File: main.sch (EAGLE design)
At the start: 26 parts, among them IC1 FT232RL, U1 ATMEGA328P_TQFP, Y3 16MHz

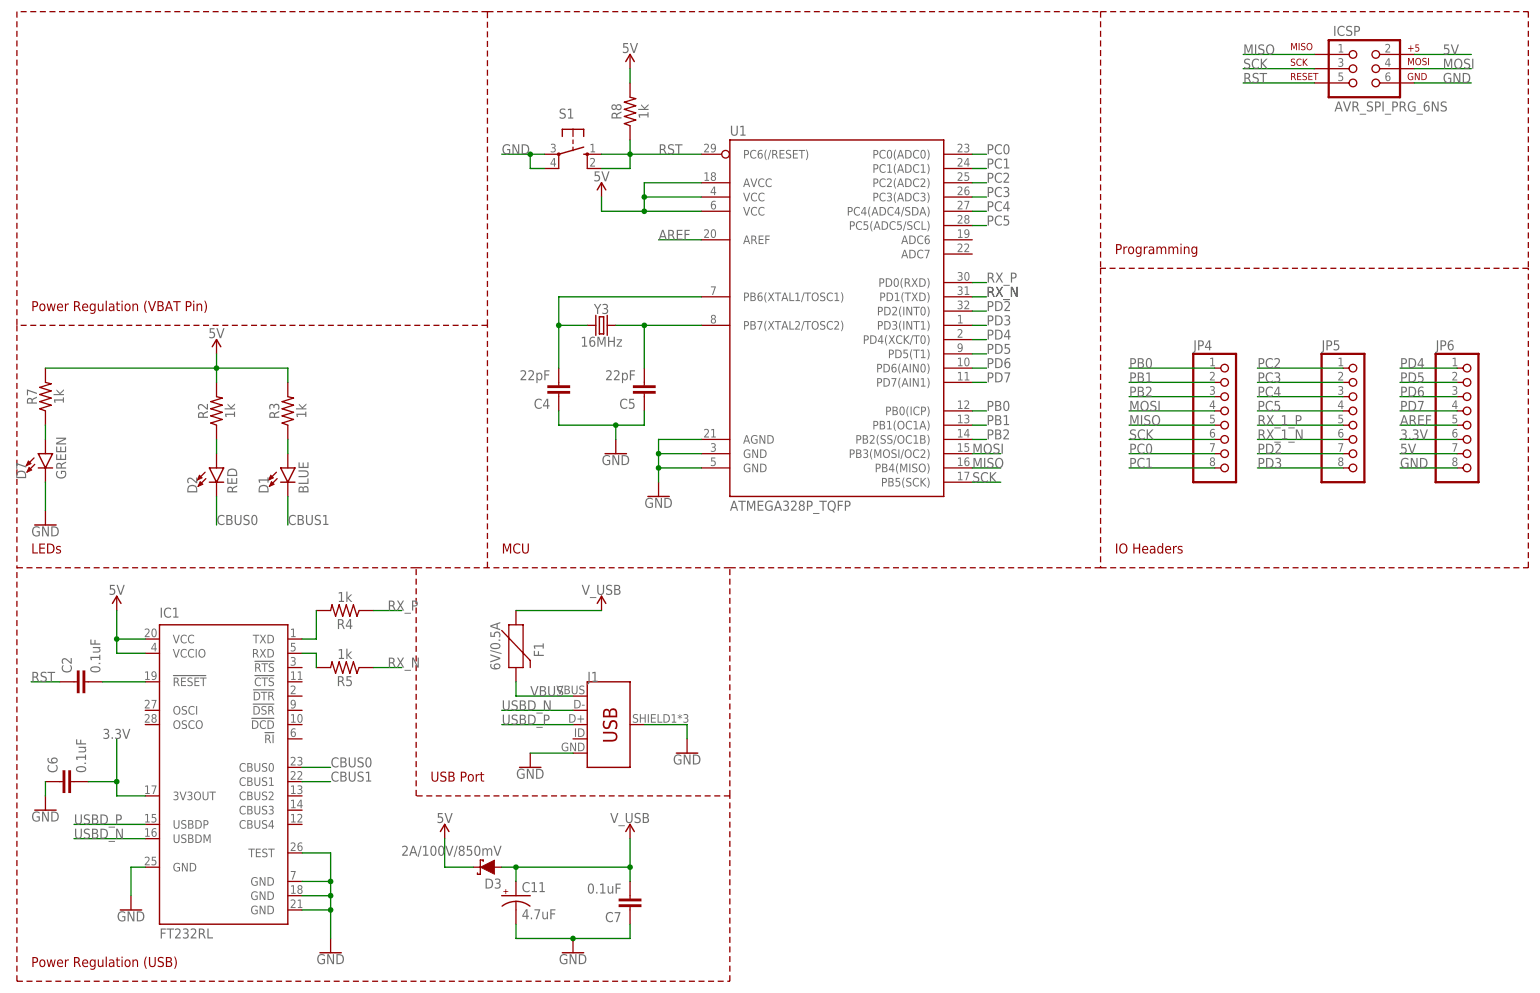
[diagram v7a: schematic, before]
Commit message: 8/1/17 - Used new ATMEGA32U4
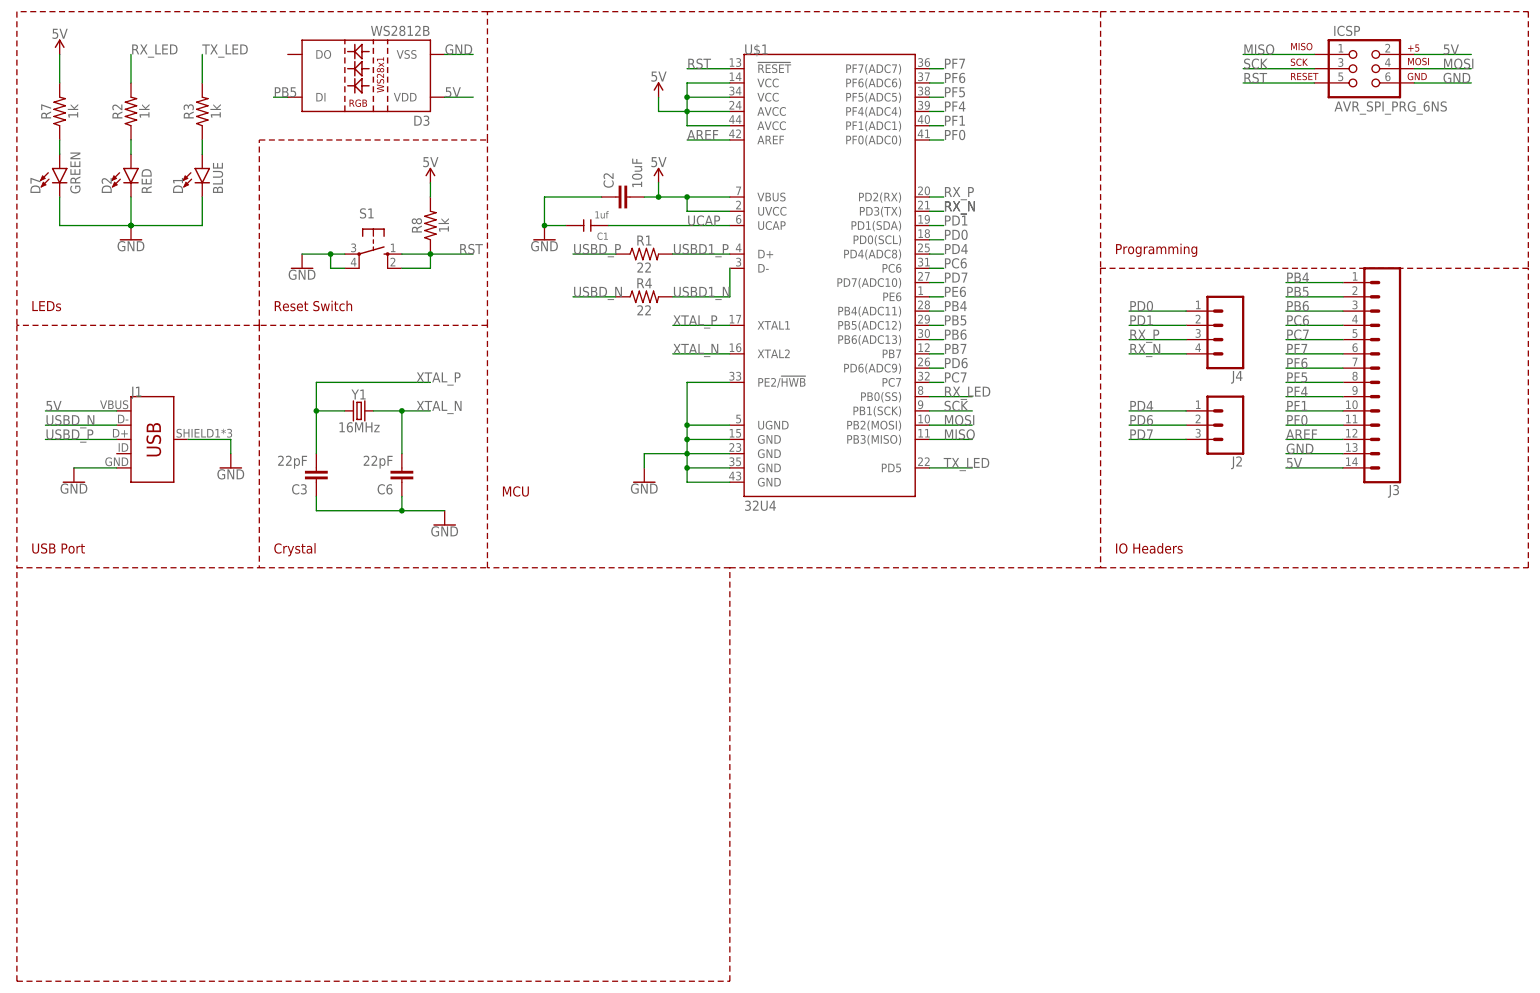
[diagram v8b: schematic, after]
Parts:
- removed C11: 4.7uF, SparkFun-Capacitors:10UF-POLAR-0603-6.3V-20%(TANT)
- removed C4, C5: 22pF, SparkFun-Capacitors:22PF-0603-50V-5%
- removed C7: 0.1uF, SparkFun-Capacitors:0.1UF-0603-25V-5%
- removed F1: 6V/0.5A, SparkFun-Fuses:PPTC_HALF-AMP
- removed IC1: FT232RL, ftdichip:FT232RL
- removed JP4, JP5, JP6: (no value), pinhead:PINHD-1X8
- removed R5: 1k, SparkFun-Resistors:RESISTOR0805
- removed U1: ATMEGA328P_TQFP, SparkFun-IC-Microcontroller:ATMEGA328P_TQFP
- removed Y3: 16MHz, SparkFun-Clocks:CRYSTAL-16MHZPTH-HC49US
- added C1: 1uf, Seeed-Capacitor:CERAMIC-1UF-25V-10%-X7R(0603)
- added C3: 22pF, SparkFun-Capacitors:22PF-0603-50V-5%
- added J2: (no value), SparkFun-Connectors:CONN_03
- added J3: (no value), SparkFun-Connectors:CONN_14
- added J4: (no value), SparkFun-Connectors:CONN_04
- added R1: 22, SparkFun-Resistors:22OHM-0603-1/10W-1%
- added U$1: 32U4, SparkFun-IC-Microcontroller:ATMEGA32U4TQFP-44
- added Y1: 16MHz, SparkFun-Clocks:CRYSTAL-16MHZPTH-HC49US
- C2: value 0.1uF -> 10uF; device SparkFun-Capacitors:0.1UF-0603-25V-5% -> SparkFun-Capacitors:10UF-0805-10V-10%
- C6: value 0.1uF -> 22pF; device SparkFun-Capacitors:0.1UF-0603-25V-5% -> SparkFun-Capacitors:22PF-0603-50V-5%
- D3: value 2A/100V/850mV -> WS2812B; device SparkFun-DiscreteSemi:DIODE-SCHOTTKY-SS14 -> SparkFun-LED:WS2812B
- R4: value 1k -> 22; device SparkFun-Resistors:RESISTOR0805 -> SparkFun-Resistors:22OHM-0603-1/10W-1%
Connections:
- removed net 3.3V: C6.2, IC1.3V3OUT, JP6.6
- removed net CBUS0: D2.C, IC1.CBUS0
- removed net CBUS1: D1.C, IC1.CBUS1
- removed net N$7: C2.2, IC1.!RESET
- removed net PB0: JP4.1, U1.PB0(ICP)
- removed net PB1: JP4.2, U1.PB1(OC1A)
- removed net PB2: JP4.3, U1.PB2(SS/OC1B)
- removed net PC0: JP4.7, U1.PC0(ADC0)
- removed net PC1: JP4.8, U1.PC1(ADC1)
- removed net PC2: JP5.1, U1.PC2(ADC2)
- removed net PC3: JP5.2, U1.PC3(ADC3)
- removed net PC4: JP5.3, U1.PC4(ADC4/SDA)
- removed net PC5: JP5.4, U1.PC5(ADC5/SCL)
- removed net PD2: JP5.7, U1.PD2(INT0)
- removed net PD3: JP5.8, U1.PD3(INT1)
- removed net PD5: JP6.2, U1.PD5(T1)
- removed net RX_1_N: IC1.RXD, JP5.6, R5.2
- removed net RX_1_P: IC1.TXD, JP5.5, R4.2
- removed net VBUS: F1.2, J1.VBUS
- removed net V_USB: C11.+, C7.2, D3.A, F1.1
- new net PB4: J3.1, U$1.PB4(ADC11)
- new net PB5: D3.DI, J3.2, U$1.PB5(ADC12)
- new net PB6: J3.3, U$1.PB6(ADC13)
- new net PB7: U$1.PB7
- new net PC6: J3.4, U$1.PC6
- new net PC7: J3.5, U$1.PC7
- new net PD0: J4.1, U$1.PD0(SCL)
- new net PD1: J4.2, U$1.PD1(SDA)
- new net PE6: U$1.PE6
- new net PF0: J3.11, U$1.PF0(ADC0)
- new net PF1: J3.10, U$1.PF1(ADC1)
- new net PF4: J3.9, U$1.PF4(ADC4)
- new net PF5: J3.8, U$1.PF5(ADC5)
- new net PF6: J3.7, U$1.PF6(ADC6)
- new net PF7: J3.6, U$1.PF7(ADC7)
- new net RX_LED: R2.2, U$1.PB0(SS)
- new net TX_LED: R3.2, U$1.PD5
- new net UCAP: C1.1, U$1.UCAP
- new net USBD1_N: R4.2, U$1.D-
- new net USBD1_P: R1.2, U$1.D+
- net 5V: now also C2.2, D3.VDD, J1.VBUS, J3.14, U$1.AVCC@24, U$1.AVCC@44, U$1.UVCC, U$1.VBUS, U$1.VCC@14, U$1.VCC@34; no longer D3.C, IC1.VCC, IC1.VCCIO, JP6.7, R2.2, R3.2, U1.AVCC, U1.VCC@4, U1.VCC@6
- net AREF: now also J3.12, U$1.AREF; no longer JP6.5, U1.AREF
- net GND: now also C1.2, C2.1, C3.1, D1.C, D2.C, D3.VSS, J3.13, U$1.GND@15, U$1.GND@23, U$1.GND@35, U$1.GND@43, U$1.PE2/!HWB, U$1.UGND; no longer C11.-, C4.1, C5.1, C7.1, IC1.GND, IC1.GND@1, IC1.GND@2, IC1.GND@A, IC1.TEST, JP6.8, U1.AGND, U1.GND@3, U1.GND@5
- net MISO: now also U$1.PB3(MISO); no longer JP4.5, U1.PB4(MISO)
- net MOSI: now also U$1.PB2(MOSI); no longer JP4.4, U1.PB3(MOSI/OC2)
- net PD4: now also J2.1, U$1.PD4(ADC8); no longer JP6.1, U1.PD4(XCK/T0)
- net PD6: now also J2.2, U$1.PD6(ADC9); no longer JP6.3, U1.PD6(AIN0)
- net PD7: now also J2.3, U$1.PD7(ADC10); no longer JP6.4, U1.PD7(AIN1)
- net RST: now also U$1.!RESET; no longer C2.1, U1.PC6(/RESET)
- net RX_N: now also J4.4, U$1.PD3(TX); no longer R5.1, U1.PD1(TXD)
- net RX_P: now also J4.3, U$1.PD2(RX); no longer R4.1, U1.PD0(RXD)
- net SCK: now also U$1.PB1(SCK); no longer JP4.6, U1.PB5(SCK)
- net USBD_N: now also R4.1; no longer IC1.USBDM
- net USBD_P: now also R1.1; no longer IC1.USBDP
- net XTAL_N: now also C6.2, U$1.XTAL2, Y1.2; no longer C5.2, U1.PB7(XTAL2/TOSC2), Y3.2
- net XTAL_P: now also C3.2, U$1.XTAL1, Y1.1; no longer C4.2, U1.PB6(XTAL1/TOSC1), Y3.1
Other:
- note added: "Crystal"
- note added: "Reset Switch"
- note removed: "Power Regulation (USB)"
- note removed: "Power Regulation (VBAT Pin)"
- moved on the sheet: C2, C6, D1, D2, D7, J1, R2, R3, R4, R7, R8, S1
